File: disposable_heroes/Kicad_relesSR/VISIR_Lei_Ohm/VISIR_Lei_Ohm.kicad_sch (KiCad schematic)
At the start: 16 parts, among them J1 Raspberry PI5, K1 3572-1220-123, K2 3572-1220-123, K3 3572-1220-123, K4 3570-1331-123, K5 3570-1331-123, K6 3570-1331-123, K7 3570-1331-123, K8 3570-1331-123, U1 74HC595N_112, U2 ULN2003

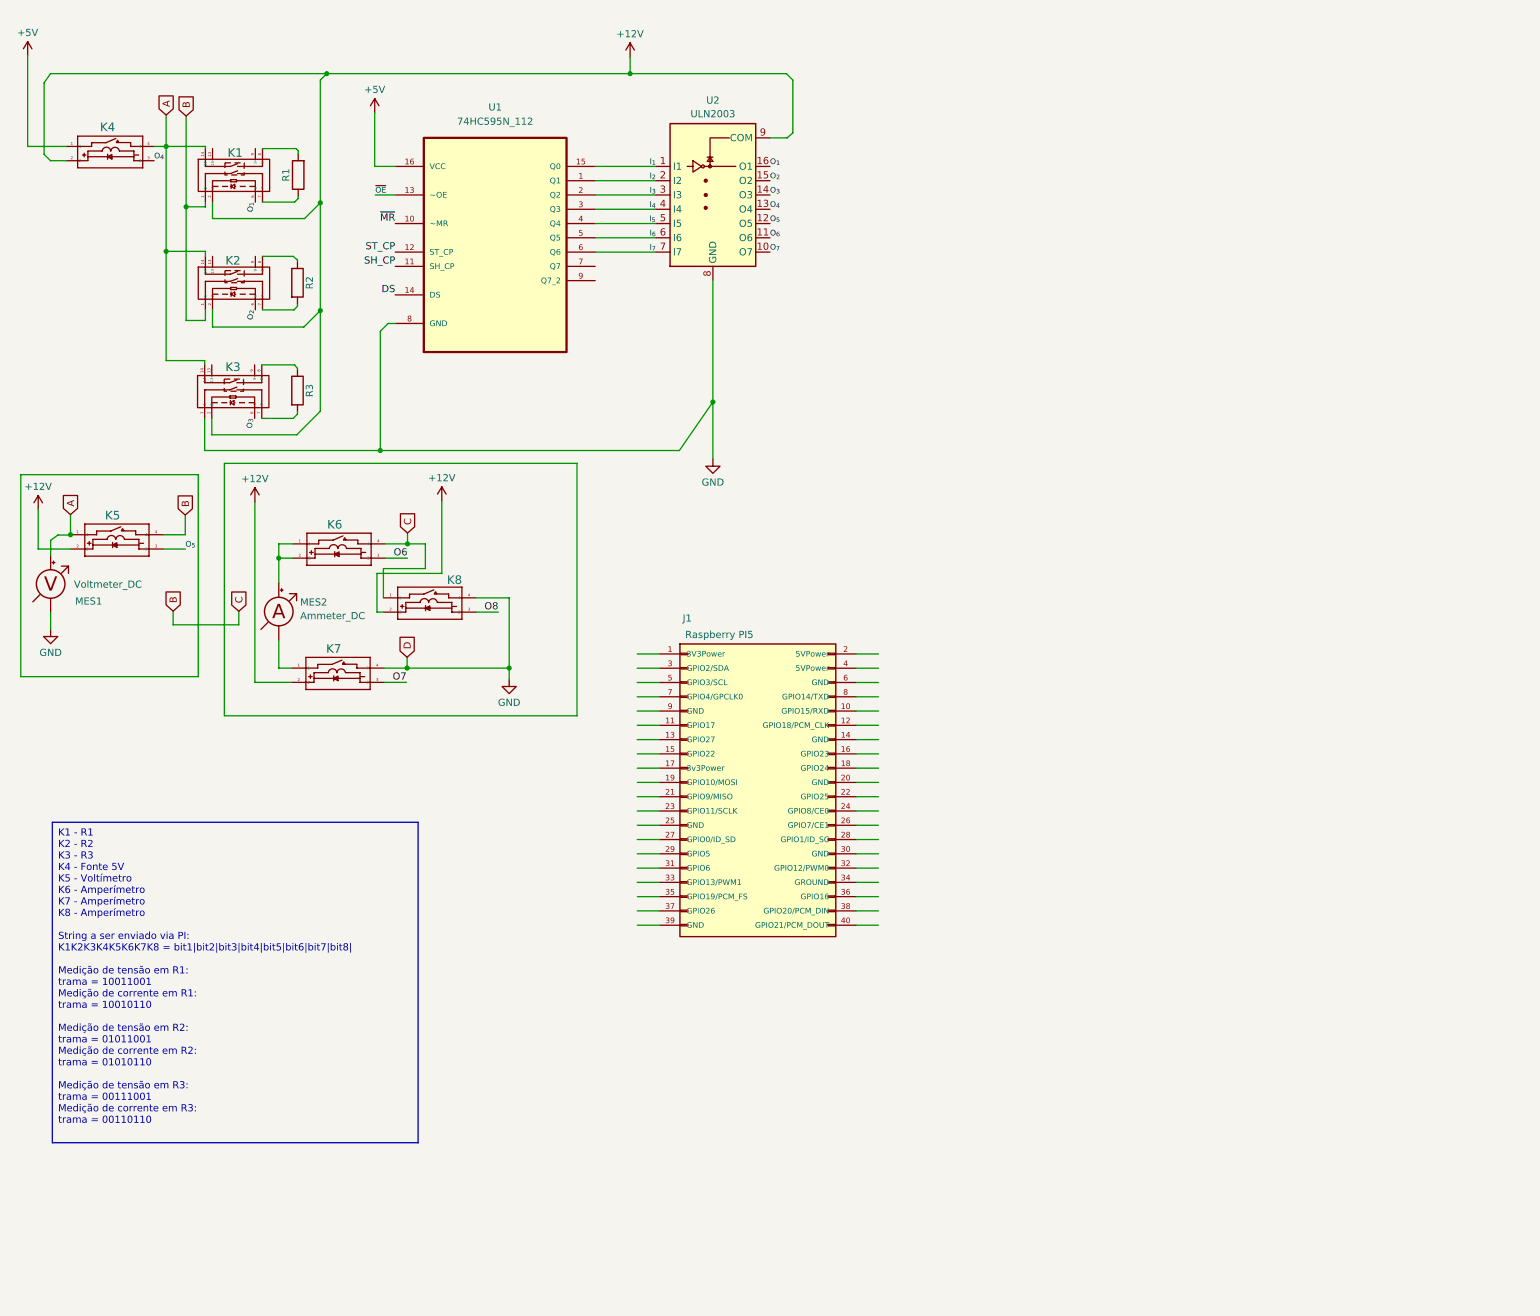
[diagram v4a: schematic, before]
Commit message: update scheme relay
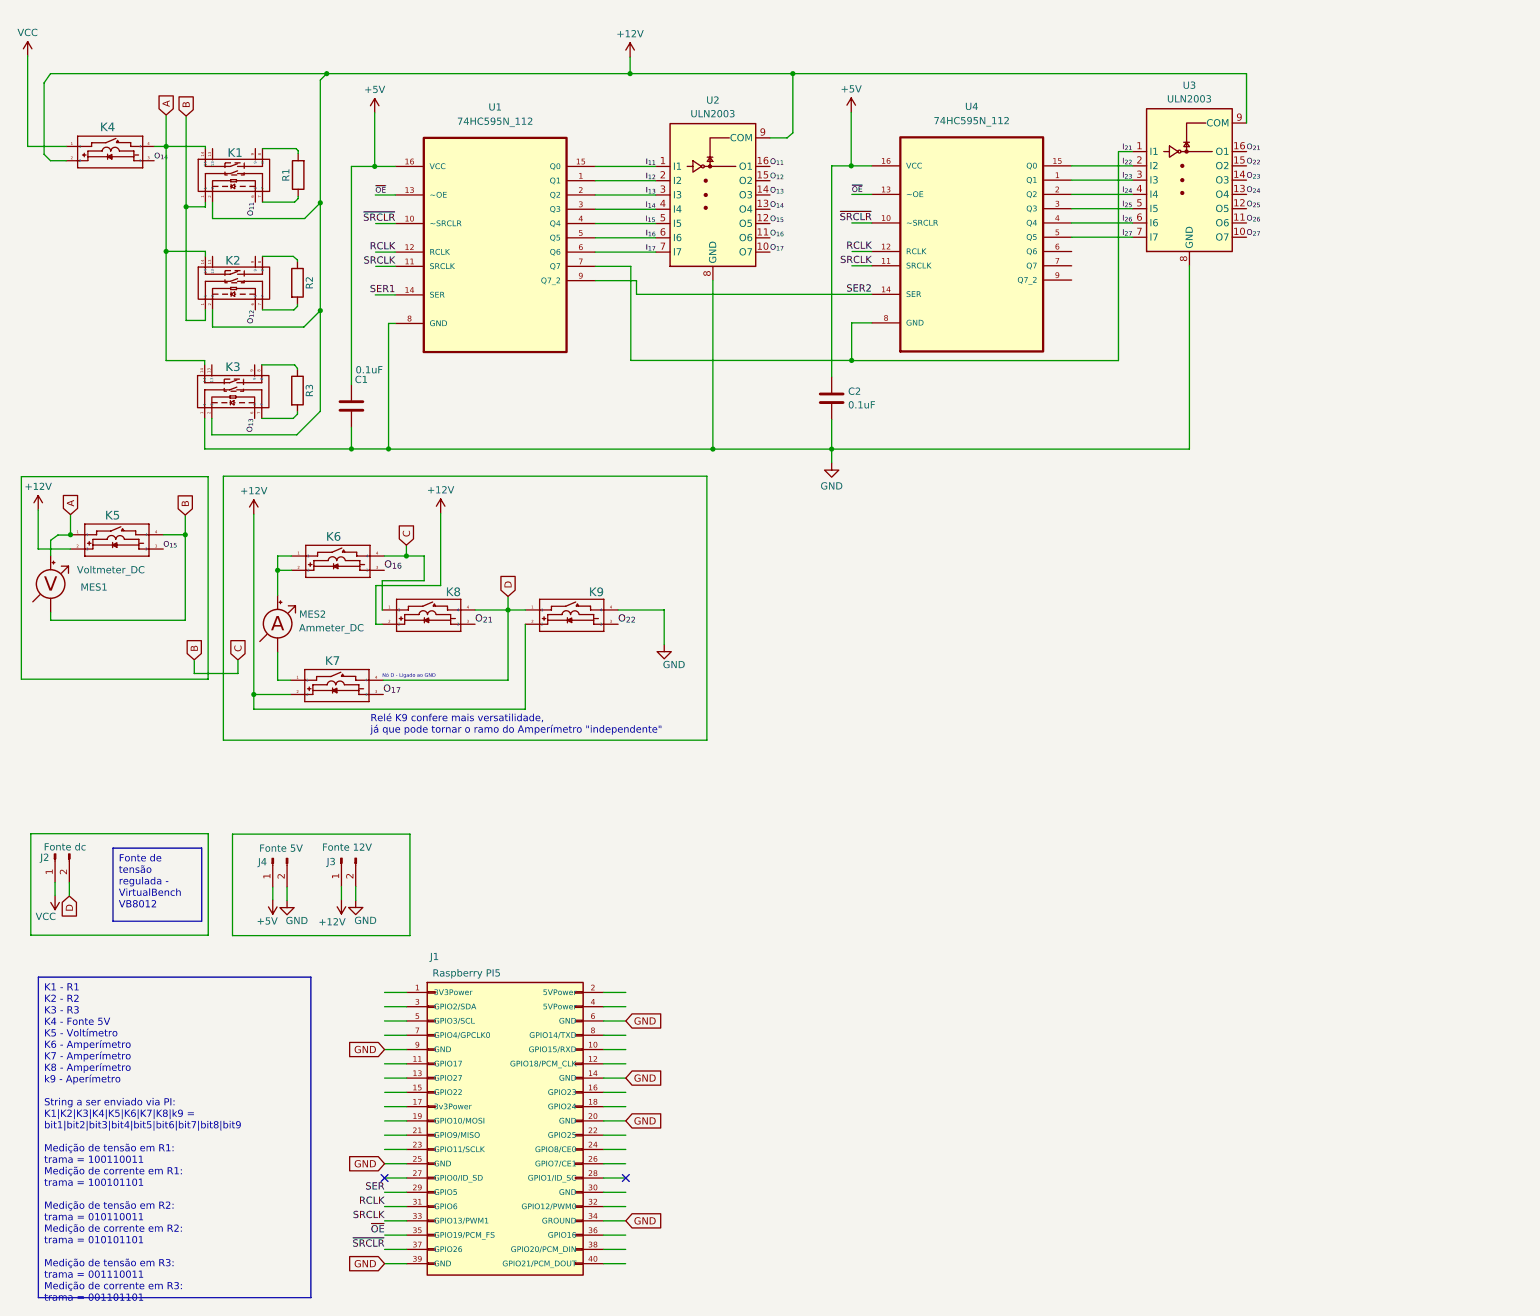
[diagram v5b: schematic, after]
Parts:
- added C1, C2: 0.1uF, symbol Device:C
- added J2: Fonte dc, Connector_PinSocket_2.54mm:PinSocket_1x02_P2.54mm_Vertical, symbol Connector:Conn_01x02_Pin
- added J3: Fonte 12V, Connector_PinSocket_2.54mm:PinSocket_1x02_P2.54mm_Vertical, symbol Connector:Conn_01x02_Pin
- added J4: Fonte 5V, Connector_PinSocket_2.54mm:PinSocket_1x02_P2.54mm_Vertical, symbol Connector:Conn_01x02_Pin
- added K9: 3570-1331-123, 3570-1220-123:SIP_3570-1331_COM, symbol 3570-1331-123:3570-1331-123
- added U3: ULN2003, Package_DIP:DIP-16_W10.16mm, symbol Transistor_Array:ULN2003
- added U4: 74HC595N_112, 74HC595N_112:DIP254P762X420-16, symbol 74HC595N:74HC595N_112
- J1: footprint (none) -> Connector_PinSocket_2.54mm:PinSocket_2x20_P2.54mm_Vertical
- K1, K2, K3: footprint rele_DPST_tese:RELAY8_3572-1220-053_COM -> 3572-1220-053:RELAY8_3572-1220-053_COM
- K4: footprint rele_SPST_tese:SIP_3570-1331_COM -> 3570-1220-123:SIP_3570-1331_COM
- K5, K6, K7, K8: footprint SIP_3570-1331_COM -> 3570-1220-123:SIP_3570-1331_COM
- MES2: footprint (none) -> Connector_PinHeader_2.54mm:PinHeader_1x02_P2.54mm_Vertical
- U1: footprint Package_DIP:DIP-16_W10.16mm -> 74HC595N_112:DIP254P762X420-16
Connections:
- net O_{6} is gone; now on net O_{16}: U2.11 (O6)
- net O_{7} is gone; now on net O_{17}: U2.10 (O7)
- net SH_CP is gone; now on net SRCLK: U1.11 (SRCLK)
- net ST_CP is gone; now on net RCLK: U1.12 (RCLK)
- net ~{MR} is gone; now on net ~{SRCLR}: U1.10 (~SRCLR)
- net +12V: now also J3.1 (Pin_1), K9.2, U3.9 (COM)
- net +5V: now also C1.1, C2.1, J4.1 (Pin_1), U4.16 (VCC); no longer K4.1
- net B: now also MES1.1 (-)
- net GND: now also J1.14 (GND), J1.20 (GND), J1.25 (GND), J1.34 (GROUND), J1.39 (GND), J1.6 (GND), J1.9 (GND), C1.2, C2.2, J3.2 (Pin_2), J4.2 (Pin_2), K9.4, U3.8 (GND); no longer K7.4, K8.4, MES1.1 (-)
- net ~{OE}: now also J1.35 (GPIO19/PCM_FS), U4.13 (~OE)
- net I_{21}: now reaches U1.7 (Q7)
- net I_{21}: now also U3.1 (I1), U4.8 (GND)
- net SER2: now reaches U1.9 (Q7_2)
- net SER2: now also U4.14 (SER)
- net SER: now reaches J1.29 (GPIO5)
- net RCLK: now reaches J1.31 (GPIO6)
- net RCLK: now also U4.12 (RCLK)
- net SRCLK: now reaches J1.33 (GPIO13/PWM1)
- net SRCLK: now also U4.11 (SRCLK)
- net ~{SRCLR}: now reaches J1.37 (GPIO26)
- net ~{SRCLR}: now also U4.10 (~SRCLR)
- net DS renamed SER1
- net I_{1} renamed I_{11}
- net I_{2} renamed I_{12}
- net I_{3} renamed I_{13}
- net I_{4} renamed I_{14}
- net I_{5} renamed I_{15}
- net I_{6} renamed I_{16}
- net I_{7} renamed I_{17}
- net O6 renamed O_{16}
- net O7 renamed O_{17}
- net O8 renamed O_{21}
- net O_{21}: now also U3.16 (O1)
- net O_{1} renamed O_{11}
- net O_{2} renamed O_{12}
- net O_{3} renamed O_{13}
- net O_{4} renamed O_{14}
- net O_{5} renamed O_{15}
- new net D: J2.2 (Pin_2), K7.4, K8.4, K9.1
- new net I_{22}: U3.2 (I2), U4.15 (Q0)
- new net I_{23}: U3.3 (I3), U4.1 (Q1)
- new net I_{24}: U3.4 (I4), U4.2 (Q2)
- new net I_{25}: U3.5 (I5), U4.3 (Q3)
- new net I_{26}: U3.6 (I6), U4.4 (Q4)
- new net I_{27}: U3.7 (I7), U4.5 (Q5)
- new net O_{22}: K9.3, U3.15 (O2)
- new net O_{23}: U3.14 (O3)
- new net O_{24}: U3.13 (O4)
- new net O_{25}: U3.12 (O5)
- new net O_{26}: U3.11 (O6)
- new net O_{27}: U3.10 (O7)
- new net VCC: J2.1 (Pin_1), K4.1
- no-connect marks 0 -> 2
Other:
- note added: "Nó D - Ligado ao GND"
- note added: "Relé K9 confere mais versatilidade, já que pode tornar o ramo do Amperímetro "independente""
- moved on the sheet: J1, K6, K7, K8, MES2

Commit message: update
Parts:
- removed K6, K9: 3570-1331-123, 3570-1220-123:SIP_3570-1331_COM, symbol 3570-1331-123:3570-1331-123
- removed MES2: Ammeter_DC, Connector_PinHeader_2.54mm:PinHeader_1x02_P2.54mm_Vertical, symbol Device:Ammeter_DC
- added K6: 3572-1220-123, 3572-1220-053:RELAY8_3572-1220-053_COM, symbol 3572-1220-123:3572-1220-123
- added MES3: Ammeter_DC, Connector_PinHeader_2.54mm:PinHeader_1x02_P2.54mm_Vertical, symbol Device:Ammeter_DC
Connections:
- net SER is gone; now on net SER1: J1.29 (GPIO5)
- net +12V: now also K6.2
- net B: now also K3.1, K6.8
- net D: now also K7.1, K6.7; no longer K7.4
- net GND: now also K7.4, U4.8 (GND); no longer K3.1
- net I_{21}: no longer U4.8 (GND)
- net I_{23}: no longer U4.1 (Q1)
- net I_{24}: no longer U4.2 (Q2)
- net I_{25}: no longer U4.3 (Q3)
- net I_{26}: no longer U4.4 (Q4)
- net I_{27}: no longer U4.5 (Q5)
- net O_{16}: now also K6.6
- net O_{17}: now also K8.3; no longer K7.3
- net O_{21}: now also K7.3; no longer K8.3
- new net: K6.1, MES3.1 (-)
- new net: K6.14, MES3.2 (+)
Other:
- moved on the sheet: J1

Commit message: update Kicad_relesSR
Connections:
- net B: no longer K5.4, MES1.1 (-)
- net D: now also K5.4, MES1.1 (-)
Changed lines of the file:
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@@
     )
   )
-  (global_label "B" (shape input) (at 42.7736 106.2228 90) (fields_autoplaced)
+  (global_label "D" (shape input) (at 42.7736 106.2228 90) (fields_autoplaced)
     (effects (font (size 1.27 1.27)) (justify left))
     (property "Intersheetrefs" "${INTERSHEET_REFS}" (at 42.7736 101.9676 90)
